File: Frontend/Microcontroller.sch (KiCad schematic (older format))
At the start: 25 parts, among them J10 SWD, Q1 ULN2003AD, U10 STM32F030C8T, U9 MAX5725AAUP

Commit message: Route PCB
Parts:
- added C113: 100n, IPC7351-Nominal:CAPC1608X55, symbol C-0603
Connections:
- net labels added: CH1_ATT1, CH1_DC, CH1_TERM, CH2_ATT1, CH2_DC, CH2_TERM
- wire segments 138 -> 153
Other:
- note removed: "GPIO"
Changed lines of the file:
@@
 	1    0    0    -1
 $EndComp
-Text Notes 1400 3300 0    60   ~ 0
-GPIO
-Text Notes 1400 3700 0    60   ~ 0
-GPIO
-Text Notes 1400 3800 0    60   ~ 0
-GPIO
-Text Notes 1400 4200 0    60   ~ 0
-GPIO
-Text Notes 1400 5200 0    60   ~ 0
-GPIO
-Text Notes 3400 5000 0    60   ~ 0
-GPIO
-Text Notes 3400 5100 0    60   ~ 0
-GPIO
-Text Notes 3400 5200 0    60   ~ 0
-GPIO
-Text Notes 3400 5300 0    60   ~ 0
-GPIO
-Text Notes 1400 5300 0    60   ~ 0
-GPIO
-Text Notes 1400 5400 0    60   ~ 0
-GPIO
-Text Notes 3400 3900 0    60   ~ 0
-GPIO
 Text Label 3400 4200 0    50   ~ 0
 #CSDAC
@@
 	9500 4000 9400 4000
 Wire Wire Line
-	8100 3300 8400 3300
-Wire Wire Line
-	8100 3400 8400 3400
-Wire Wire Line
-	8100 3500 8400 3500
-Wire Wire Line
-	8100 3600 8400 3600
-Wire Wire Line
-	8100 3700 8400 3700
-Wire Wire Line
-	8100 3800 8400 3800
+	7900 3300 8400 3300
+Wire Wire Line
+	7900 3400 8400 3400
+Wire Wire Line
+	7900 3500 8400 3500
+Wire Wire Line
+	7900 3600 8400 3600
+Wire Wire Line
+	7900 3700 8400 3700
+Wire Wire Line
+	7900 3800 8400 3800
 Wire Wire Line
 	9500 3100 9400 3100
@@
 F1 "LevelShifters.sch" 60
 F2 "VREF_IN" I L 8300 1300 50
-F3 "VOS1_CH1_IN" I L 8300 1600 50
+F3 "VOS1_CH1_IN" I L 8300 1800 50
 F4 "VOS2_CH1_IN" I L 8300 1700 50
-F5 "VOS3_CH1_IN" I L 8300 1800 50
+F5 "VOS3_CH1_IN" I L 8300 1600 50
 F6 "VOS1_CH2_IN" I L 8300 1900 50
 F7 "VOS2_CH2_IN" I L 8300 2000 50
@@
 Wire Wire Line
 	8300 1300 7900 1300
-Wire Wire Line
-	7900 1600 8300 1600
-Wire Wire Line
-	7900 1700 8300 1700
-Wire Wire Line
-	7900 1800 8300 1800
-Wire Wire Line
-	7900 1900 8300 1900
-Wire Wire Line
-	7900 2000 8300 2000
-Wire Wire Line
-	7900 2100 8300 2100
 Text HLabel 9900 1600 2    50   Output ~ 0
 VOS1_CH1
@@
 Text Label 5800 1000 0    50   ~ 0
 3V3DAC
-Text Notes 3400 3800 0    60   ~ 0
-GPIO
-Text Notes 3400 3700 0    60   ~ 0
-GPIO
-Text Notes 3400 3500 0    60   ~ 0
-GPIO
-Text Notes 3400 2700 0    50   ~ 0
-ADC
 $Comp
 L C-TANT-3528-21 C37
@@
 	1    0    0    -1
 $EndComp
-Text Notes 3400 2800 0    50   ~ 0
-ADC
 Text Notes 3400 2900 0    50   ~ 0
 ADC
@@
 Wire Wire Line
 	1550 1250 1550 1200
-Text HLabel 9900 4500 2    50   Output ~ 0
+Text HLabel 3700 4500 2    50   Output ~ 0
 CH1_ATT2
-Text HLabel 9900 4600 2    50   Output ~ 0
+Text HLabel 3700 4400 2    50   Output ~ 0
 CH1_GAIN1
-Text HLabel 9900 4700 2    50   Output ~ 0
+Text HLabel 3700 4600 2    50   Output ~ 0
 CH1_GAIN2
-Text HLabel 9900 4900 2    50   Output ~ 0
+Text HLabel 1600 5200 0    50   Output ~ 0
 CH2_ATT2
-Text HLabel 9900 5000 2    50   Output ~ 0
+Text HLabel 1600 4200 0    50   Output ~ 0
 CH2_GAIN1
-Text HLabel 9900 5100 2    50   Output ~ 0
+Text HLabel 1600 3800 0    50   Output ~ 0
 CH2_GAIN2
-Text HLabel 9900 5400 0    50   Input ~ 0
+Text HLabel 3400 2800 2    50   Input ~ 0
 CH1_TEMP
-Text HLabel 9900 5500 0    50   Input ~ 0
+Text HLabel 3400 2700 2    50   Input ~ 0
 CH2_TEMP
+$Comp
+L C-0603 C113
+U 1 1 5551B6DA
+P 6100 1250
+F 0 "C113" H 5900 1200 50  0000 C CNN
+F 1 "100n" H 5900 1300 50  0000 C CNN
+F 2 "IPC7351-Nominal:CAPC1608X55" H 6100 1250 50  0001 C CNN
+F 3 "" H 6090 1225 60  0000 C CNN
+F 4 "Value" H 6100 1250 60  0001 C CNN "Manuf"
+F 5 "CAP MLCC 100pF C0G 50V 5% [0603]" H 6900 1800 60  0001 C CNN "BOM"
+	1    6100 1250
+	-1   0    0    1
+$EndComp
+$Comp
+L +3.3 #PWR0169
+U 1 1 5551B75B
+P 6100 1150
+F 0 "#PWR0169" H 6100 1200 30  0001 C CNN
+F 1 "+3.3" H 6100 1250 50  0000 C CNN
+F 2 "" H 6100 1150 60  0000 C CNN
+F 3 "" H 6100 1150 60  0000 C CNN
+	1    6100 1150
+	1    0    0    -1
+$EndComp
+$Comp
+L GND #PWR0170
+U 1 1 5551B7C1
+P 6100 1400
+F 0 "#PWR0170" H 6100 1400 30  0001 C CNN
+F 1 "GND" H 6100 1330 30  0001 C CNN
+F 2 "" H 6100 1400 60  0000 C CNN
+F 3 "" H 6100 1400 60  0000 C CNN
+	1    6100 1400
+	1    0    0    -1
+$EndComp
+Wire Wire Line
+	6100 1400 6100 1350
+Wire Wire Line
+	8300 1600 7900 1600
+Wire Wire Line
+	8300 1700 7900 1700
+Wire Wire Line
+	8300 1800 7900 1800
+Wire Wire Line
+	7900 1900 8300 1900
+Wire Wire Line
+	7900 2000 8300 2000
+Wire Wire Line
+	7900 2100 8300 2100
+Text Label 7900 3300 0    50   ~ 0
+CH1_TERM
+Text Label 7900 3400 0    50   ~ 0
+CH1_DC
+Text Label 7900 3500 0    50   ~ 0
+CH1_ATT1
+Text Label 7900 3600 0    50   ~ 0
+CH2_TERM
+Text Label 7900 3700 0    50   ~ 0
+CH2_DC
+Text Label 7900 3800 0    50   ~ 0
+CH2_ATT1
+Text Label 3800 3900 2    50   ~ 0
+CH2_ATT1
+Wire Wire Line
+	3800 3900 3300 3900
+Text Label 3800 3800 2    50   ~ 0
+CH2_DC
+Wire Wire Line
+	3800 3800 3300 3800
+Text Label 3800 3700 2    50   ~ 0
+CH2_TERM
+Wire Wire Line
+	3800 3700 3300 3700
+Text Label 3800 5000 2    50   ~ 0
+CH1_ATT1
+Wire Wire Line
+	3800 5000 3300 5000
+Text Label 3800 5100 2    50   ~ 0
+CH1_DC
+Text Label 3800 5200 2    50   ~ 0
+CH1_TERM
+Wire Wire Line
+	3800 5200 3300 5200
+Wire Wire Line
+	3800 5100 3300 5100
+Wire Wire Line
+	3700 4600 3300 4600
+Wire Wire Line
+	3700 4500 3300 4500
+Wire Wire Line
+	3700 4400 3300 4400
+Wire Wire Line
+	3400 2800 3300 2800
+Wire Wire Line
+	3400 2700 3300 2700
+Wire Wire Line
+	1600 5200 1700 5200
+Wire Wire Line
+	1600 3800 1700 3800
+Wire Wire Line
+	1600 4200 1700 4200
 $EndSCHEMATC

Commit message: Work more on routing
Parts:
- added DS1, DS10, DS11, DS12, DS2, DS3, DS4, DS5, DS6, DS7, DS8, DS9: LED-0603, smd-semi:LED-0603, symbol LED-0603
- added R128, R129, R130, R131, R132, R133, R134, R135, R136, R137, R138, R139: 3k3, IPC7351-Nominal:RESC1005X40, symbol R-0402
- TP1: footprint (none) -> conn-test:TEST-SMD-SMALL
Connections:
- net CH1_ATT1: now also R130.1
- net CH1_ATT2: now also R135.1
- net CH1_DC: now also R129.1
- net CH1_GAIN1: now also R134.1
- net CH1_GAIN2: now also R136.1
- net CH1_TERM: now also R128.1
- net CH2_ATT1: now also R133.1
- net CH2_ATT2: now also R137.1
- net CH2_DC: now also R132.1
- net CH2_GAIN1: now also R139.1
- net CH2_GAIN2: now also R138.1
- net CH2_TERM: now also R131.1
- net GND: now also DS1.1, DS10.1, DS11.1, DS12.1, DS2.1, DS3.1, DS4.1, DS5.1, DS6.1, DS7.1, DS8.1, DS9.1
- new net: DS1.2, R128.2
- new net: DS2.2, R129.2
- new net: DS3.2, R130.2
- new net: DS4.2, R131.2
- new net: DS5.2, R132.2
- new net: DS6.2, R133.2
- new net: DS7.2, R134.2
- new net: DS8.2, R135.2
- new net: DS9.2, R136.2
- new net: DS10.2, R137.2
- new net: DS11.2, R138.2
- new net: DS12.2, R139.2

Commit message: More layout work
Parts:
- removed C43, C45: 15u/16, IPC7351-Nominal:CAPMP3528X210, symbol C-TANT-3528-21
- removed C46: 1u, IPC7351-Nominal:CAPC2012X70, symbol C-0805
- added C43, C45: 2u2, IPC7351-Nominal:CAPMP2013X120, symbol C-TANT-2012-12
- added R144, R146, R147: 3k3, IPC7351-Nominal:RESC1005X40, symbol R-0402
- added R145: 1k, IPC7351-Nominal:RESC1005X40, symbol R-0402
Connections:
- net +3.3: now also R145.1
- net 3V3ADC: now also C45.1
- net 3V3DAC: now also C43.1
- net GND: now also C43.2, C45.2, R146.2
- net +5VMON: now reaches U10.12 (PA2)
- net +5VMON: now also R144.2, R146.1
- net -5VMON: now reaches U10.13 (PA3)
- net -5VMON: now also R145.2, R147.1
- net TEMP_VRELAY: now reaches U10.14 (PA4)
- net TEMP_V5: now reaches U10.15 (PA5)
- new net +5: R144.1
- new net -5: R147.2
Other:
- note removed: "ADC"

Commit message: Schematic touchups
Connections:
- no-connect marks 3 -> 14
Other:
- moved on the sheet: C113, C37, C38, C39, C40, C41, C42, C43, C44, C45, C47, DS1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

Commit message: Route #IRQ and #PERST
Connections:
- net #IRQ: now also U10.16 (PA6)
- net #PERST: now also U10.17 (PA7)
- no-connect marks 14 -> 12
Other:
- moved on the sheet: TP1
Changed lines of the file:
@@
 LIBS:Altera
 LIBS:conn-te
+LIBS:Vishay
+LIBS:semi-trans-OnSemi
 LIBS:frontend-cache
 EELAYER 25 0
@@
 L TESTPOINT TP1
 U 1 1 552D08AF
-P 4100 3800
-F 0 "TP1" V 3900 3950 50  0000 C CNN
-F 1 "INFO" V 4000 3950 50  0000 C CNN
-F 2 "conn-test:TEST-SMD-SMALL" H 4100 3800 50  0001 C CNN
-F 3 "" H 4100 3800 50  0000 C CNN
-	1    4100 3800
+P 4400 3800
+F 0 "TP1" V 4200 3950 50  0000 C CNN
+F 1 "INFO" V 4300 3950 50  0000 C CNN
+F 2 "conn-test:TEST-SMD-SMALL" H 4400 3800 50  0001 C CNN
+F 3 "" H 4400 3800 50  0000 C CNN
+	1    4400 3800
 	0    1    1    0
 $EndComp
@@
 	1    0    0    -1
 $EndComp
-Text HLabel 1500 6300 0    50   Output ~ 0
+Text HLabel 4100 3500 2    50   Output ~ 0
 #IRQ
 $Comp
@@
 	5600 1850 5600 1900
 Wire Wire Line
-	4100 3800 3800 3800
+	4400 3800 3800 3800
 Wire Wire Line
 	1700 6850 4300 6850
@@
 Wire Wire Line
 	8200 2300 7800 2300
-NoConn ~ 3800 3500
-NoConn ~ 3800 3600
 NoConn ~ 3800 3700
 NoConn ~ 2200 3500
@@
 	1    0    0    -1
 $EndComp
-Text HLabel 1500 6400 0    50   Input ~ 0
+Text HLabel 4100 3600 2    50   Input ~ 0
 #PERST
+Wire Wire Line
+	4100 3500 3800 3500
+Wire Wire Line
+	4100 3600 3800 3600
 $EndSCHEMATC

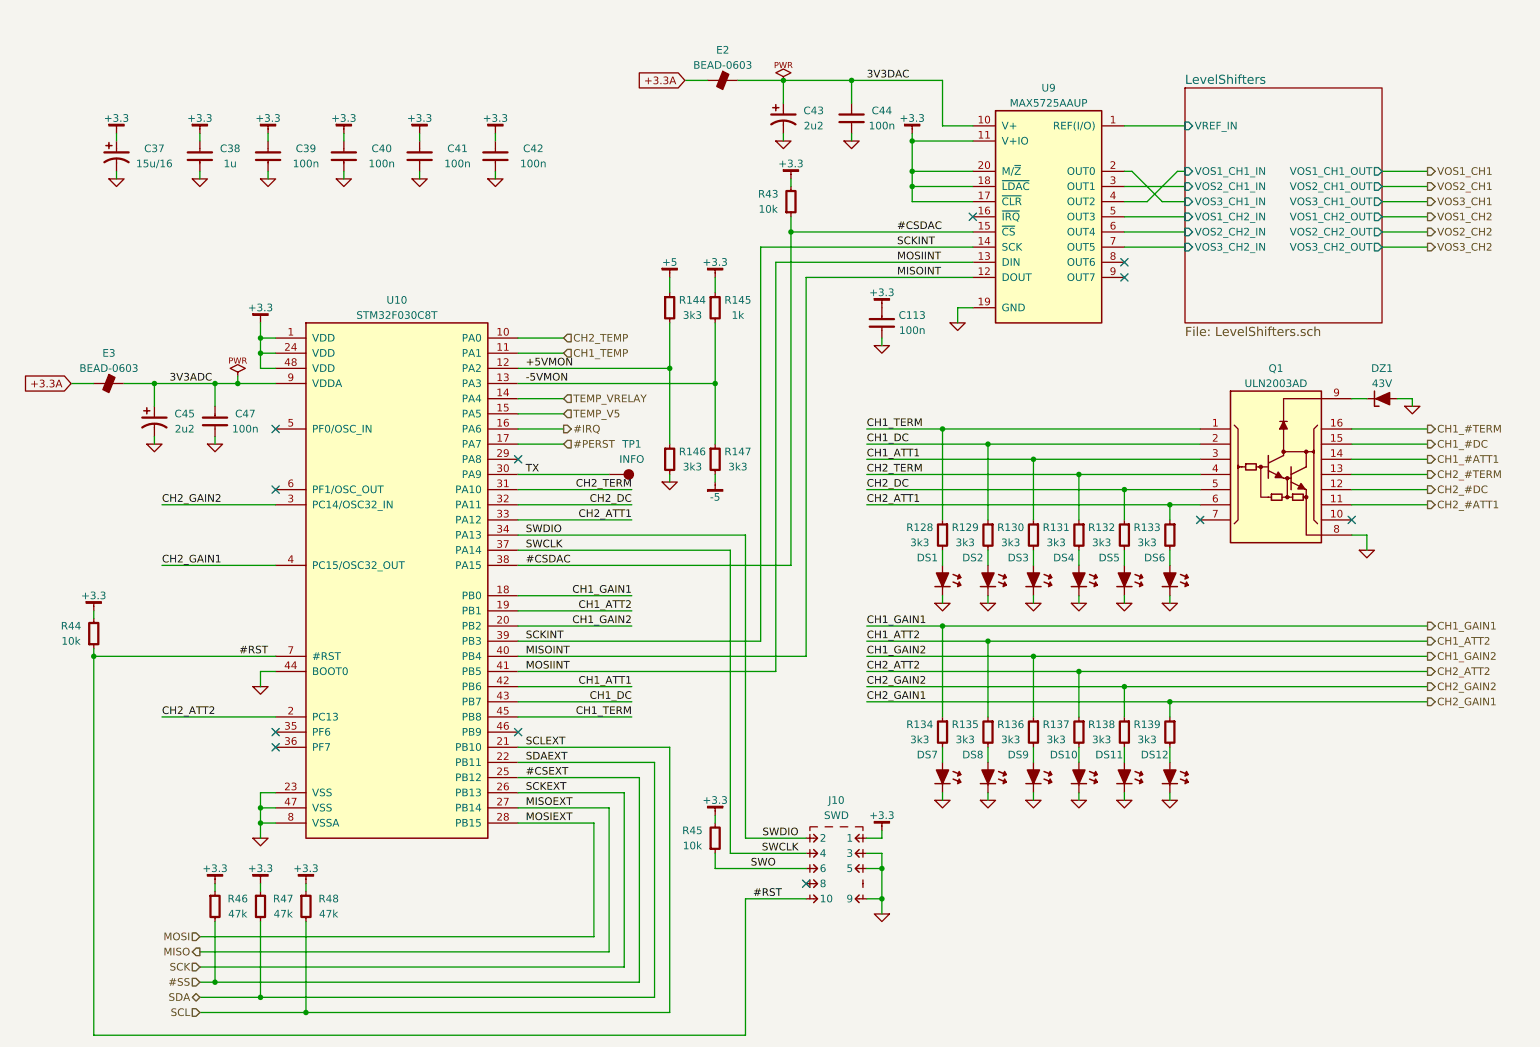
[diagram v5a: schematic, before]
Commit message: Reannotate schematic/PCB
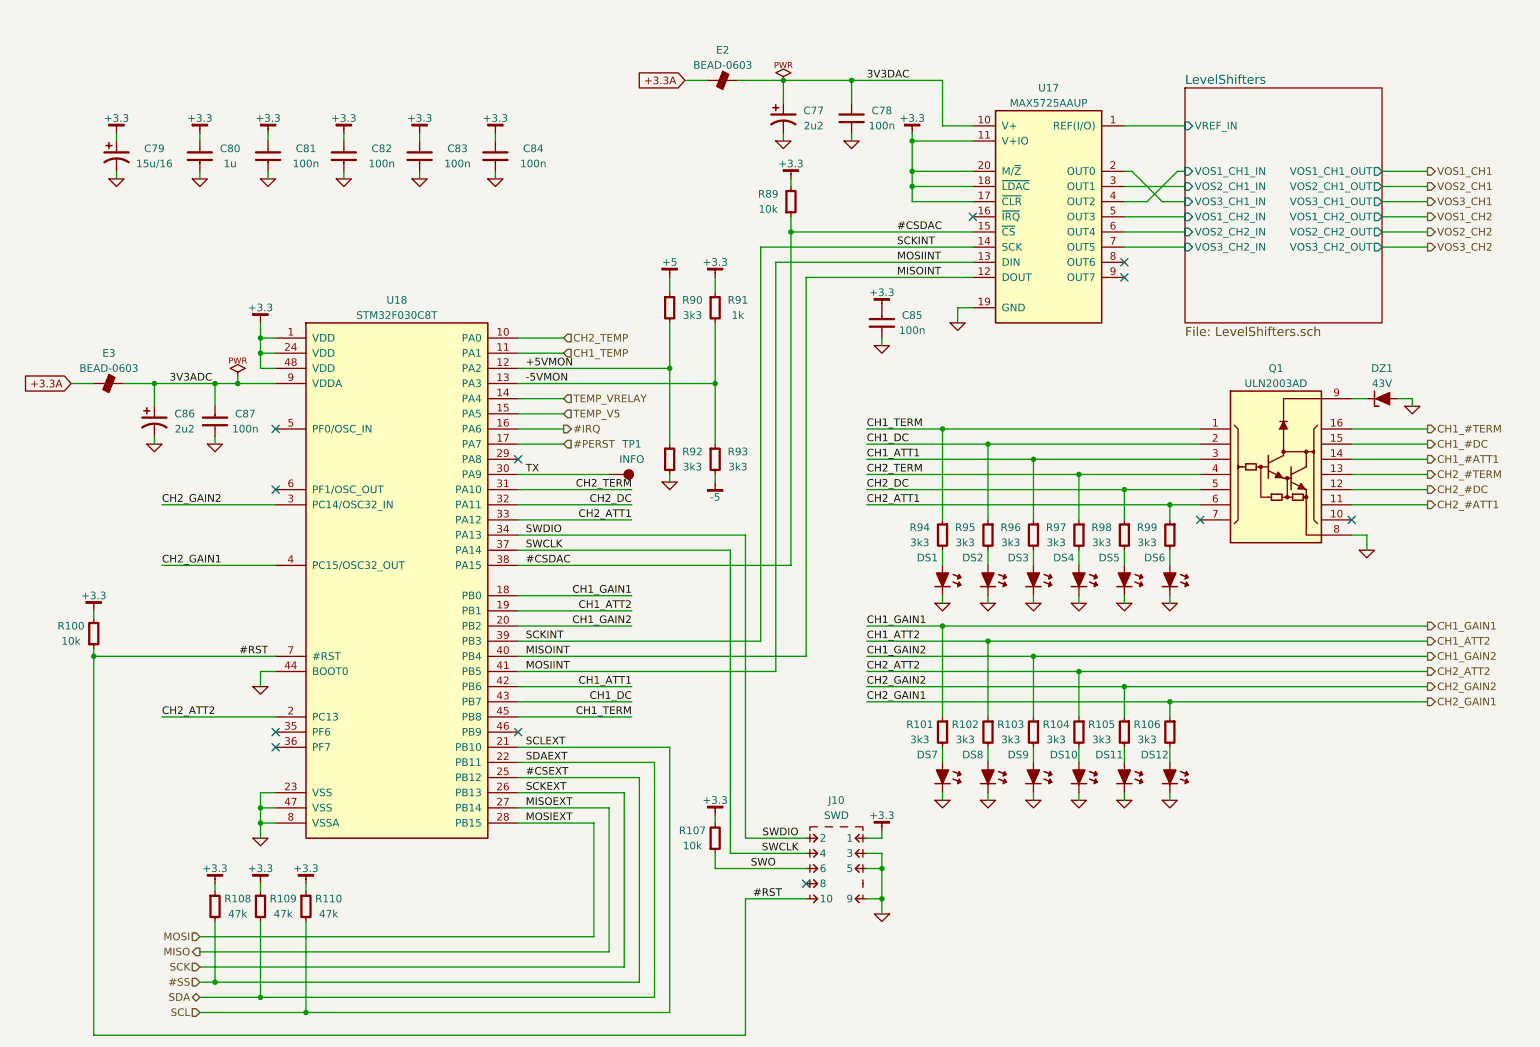
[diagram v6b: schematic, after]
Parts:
- renumbered C43 to C77, C44 to C78, C37 to C79, C38 to C80, C39 to C81, C40 to C82, C41 to C83, C42 to C84, C113 to C85, C45 to C86, C47 to C87, R44 to R100, R134 to R101, R135 to R102, R136 to R103, R137 to R104, R138 to R105, R139 to R106, R45 to R107, R46 to R108, R47 to R109, R48 to R110, R43 to R89, R144 to R90, R145 to R91, R146 to R92, R147 to R93, R128 to R94, R129 to R95, R130 to R96, R131 to R97, R132 to R98, R133 to R99, U9 to U17, U10 to U18

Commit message: Reannotate after adding parts
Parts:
- renumbered C77 to C79, C78 to C80, C79 to C81, C80 to C82, C81 to C83, C82 to C84, C83 to C85, C84 to C86, C85 to C87, C86 to C88, C87 to C89
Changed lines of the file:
@@
 AR Path="/54E51D33/5544FB83" Ref="C?"  Part="1"
 AR Path="/552E2A83/5544FB83" Ref="C?"  Part="1"
-AR Path="/552B011F/5544FB83" Ref="C81"  Part="1"
-F 0 "C81" H 2400 1750 50  0000 C CNN
+AR Path="/552B011F/5544FB83" Ref="C83"  Part="1"
+F 0 "C83" H 2400 1750 50  0000 C CNN
 F 1 "100n" H 2400 1650 50  0000 C CNN
 F 2 "IPC7351-Nominal:CAPC1608X55" H 2150 1700 50  0001 C CNN
@@
 AR Path="/54E51D33/5544FD79" Ref="C?"  Part="1"
 AR Path="/552E2A83/5544FD79" Ref="C?"  Part="1"
-AR Path="/552B011F/5544FD79" Ref="C82"  Part="1"
-F 0 "C82" H 2900 1750 50  0000 C CNN
+AR Path="/552B011F/5544FD79" Ref="C84"  Part="1"
+F 0 "C84" H 2900 1750 50  0000 C CNN
 F 1 "100n" H 2900 1650 50  0000 C CNN
 F 2 "IPC7351-Nominal:CAPC1608X55" H 2650 1700 50  0001 C CNN
@@
 AR Path="/54E51D33/5544FE55" Ref="C?"  Part="1"
 AR Path="/552E2A83/5544FE55" Ref="C?"  Part="1"
-AR Path="/552B011F/5544FE55" Ref="C83"  Part="1"
-F 0 "C83" H 3400 1750 50  0000 C CNN
+AR Path="/552B011F/5544FE55" Ref="C85"  Part="1"
+F 0 "C85" H 3400 1750 50  0000 C CNN
 F 1 "100n" H 3400 1650 50  0000 C CNN
 F 2 "IPC7351-Nominal:CAPC1608X55" H 3150 1700 50  0001 C CNN
@@
 AR Path="/54E51D33/5544FE6B" Ref="C?"  Part="1"
 AR Path="/552E2A83/5544FE6B" Ref="C?"  Part="1"
-AR Path="/552B011F/5544FE6B" Ref="C84"  Part="1"
-F 0 "C84" H 3900 1750 50  0000 C CNN
+AR Path="/552B011F/5544FE6B" Ref="C86"  Part="1"
+F 0 "C86" H 3900 1750 50  0000 C CNN
 F 1 "100n" H 3900 1650 50  0000 C CNN
 F 2 "IPC7351-Nominal:CAPC1608X55" H 3650 1700 50  0001 C CNN
@@
 NoConn ~ 6800 2100
 $Comp
-L C-0603 C78
+L C-0603 C80
 U 1 1 5546AFC9
 P 6000 1450
-F 0 "C78" H 5800 1400 50  0000 C CNN
+F 0 "C80" H 5800 1400 50  0000 C CNN
 F 1 "100n" H 5800 1500 50  0000 C CNN
 F 2 "IPC7351-Nominal:CAPC1608X55" H 6000 1450 50  0001 C CNN
@@
 3V3DAC
 $Comp
-L C-TANT-3528-21 C79
+L C-TANT-3528-21 C81
 U 1 1 55526688
 P 1150 1700
-F 0 "C79" H 1400 1750 50  0000 C CNN
+F 0 "C81" H 1400 1750 50  0000 C CNN
 F 1 "15u/16" H 1400 1650 50  0000 C CNN
 F 2 "IPC7351-Nominal:CAPMP3528X210" H 1150 1700 50  0001 C CNN
@@
 +3.3A
 $Comp
-L C-0603 C87
+L C-0603 C89
 U 1 1 555367A3
 P 1800 3450
-F 0 "C87" H 1600 3400 50  0000 C CNN
+F 0 "C89" H 1600 3400 50  0000 C CNN
 F 1 "100n" H 1600 3500 50  0000 C CNN
 F 2 "IPC7351-Nominal:CAPC1608X55" H 1800 3450 50  0001 C CNN
@@
 P 1700 1700
 AR Path="/552F27A6/5555493C" Ref="C?"  Part="1"
-AR Path="/552B011F/5555493C" Ref="C80"  Part="1"
-F 0 "C80" H 1900 1750 50  0000 C CNN
+AR Path="/552B011F/5555493C" Ref="C82"  Part="1"
+F 0 "C82" H 1900 1750 50  0000 C CNN
 F 1 "1u" H 1900 1650 50  0000 C CNN
 F 2 "IPC7351-Nominal:CAPC2012X70" H 1700 1700 50  0001 C CNN
@@
 CH2_TEMP
 $Comp
-L C-0603 C85
+L C-0603 C87
 U 1 1 5551B6DA
 P 6200 2800
-F 0 "C85" H 6000 2750 50  0000 C CNN
+F 0 "C87" H 6000 2750 50  0000 C CNN
 F 1 "100n" H 6000 2850 50  0000 C CNN
 F 2 "IPC7351-Nominal:CAPC1608X55" H 6200 2800 50  0001 C CNN
@@
 TEMP_V5
 $Comp
-L C-TANT-2012-12 C77
+L C-TANT-2012-12 C79
 U 1 1 555477E5
 P 5550 1450
-F 0 "C77" H 5750 1500 50  0000 C CNN
+F 0 "C79" H 5750 1500 50  0000 C CNN
 F 1 "2u2" H 5750 1400 50  0000 C CNN
 F 2 "IPC7351-Nominal:CAPMP2013X120" H 5550 1450 50  0001 C CNN
@@
 $EndComp
 $Comp
-L C-TANT-2012-12 C86
+L C-TANT-2012-12 C88
 U 1 1 5554B270
 P 1400 3450
-F 0 "C86" H 1600 3500 50  0000 C CNN
+F 0 "C88" H 1600 3500 50  0000 C CNN
 F 1 "2u2" H 1600 3400 50  0000 C CNN
 F 2 "IPC7351-Nominal:CAPMP2013X120" H 1400 3450 50  0001 C CNN
